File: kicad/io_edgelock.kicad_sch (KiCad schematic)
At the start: 35 parts, among them J1 EdgeLock J1, J2 EdgeLock J2, J3 EdgeLock J3, J4 EdgeLock J4, J5 EdgeLock J5, J6 EdgeLock J6, J9 EdgeLock J9

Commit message: Pick JLCPCB parts for the whole BOM and add BOM/CPL generation
Adds bom/parts.csv (LCSC numbers and MPNs), scripts to apply it to the schematic and
board and to generate the JLCPCB BOM, CPL and a live stock report. Swaps the
BOOTSEL/RESET switch to a basic 5.1 mm part with a matching footprint, and replaces
out-of-stock parts (SS54, WS2812B, 10u caps, SWD header).

Co-Authored-By: Claude Sonnet 5.5 <noreply@anthropic.com>
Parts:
- R44, R45, R46, R47, R48, R49, R50, R51, R52, R53, R54, R55, R56, R57, R58, R59, R60, R61, R62, R63, R64, R65, R66, R67, R68, R69, R70, R71: LCSC (none) -> C25076; MPN (none) -> 0402WGF1000TCE

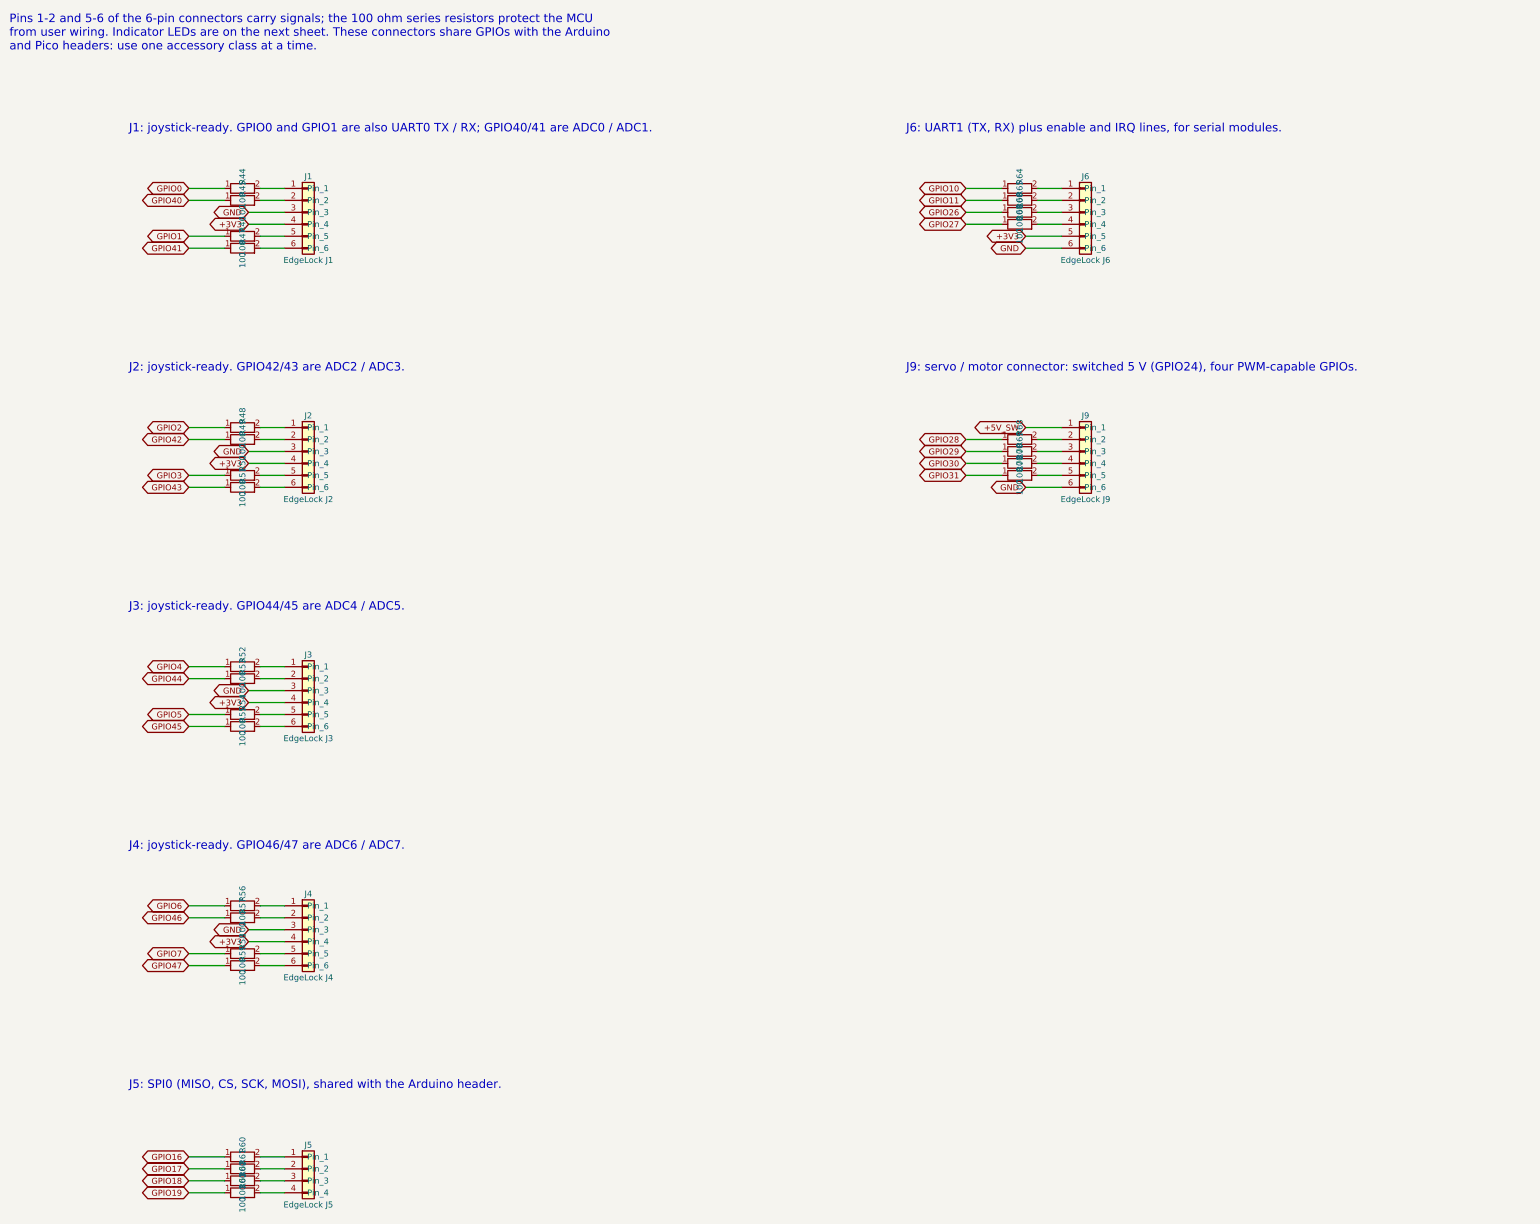
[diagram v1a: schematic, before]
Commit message: Rework board layout, swap SWD header to through-hole, add Qwiic port
- SWD (J10) is now a 1x3 2.54 mm through-hole pin header footprint
  (SWCLK, GND, SWDIO) instead of the JST SH connector; removed from the
  JLCPCB BOM.
- Add J20 Qwiic connector (XY-SM04B-SRSS-TB) on the I2C bus: GND, +3V3,
  GPIO20 (SDA), GPIO21 (SCL), mounting tabs to GND.
- Placement/routing progress and the helper scripts used for it.

DRC still reports open items (unrouted RUN/GPIO24/GPIO29/QSPI_SD0 nets,
R108/GPIO23 and NT1/GPIO20 shorts, J12 edge clearance, silkscreen
overlaps); to be fixed in follow-up commits.

Co-Authored-By: Claude Sonnet 5.5 <noreply@anthropic.com>
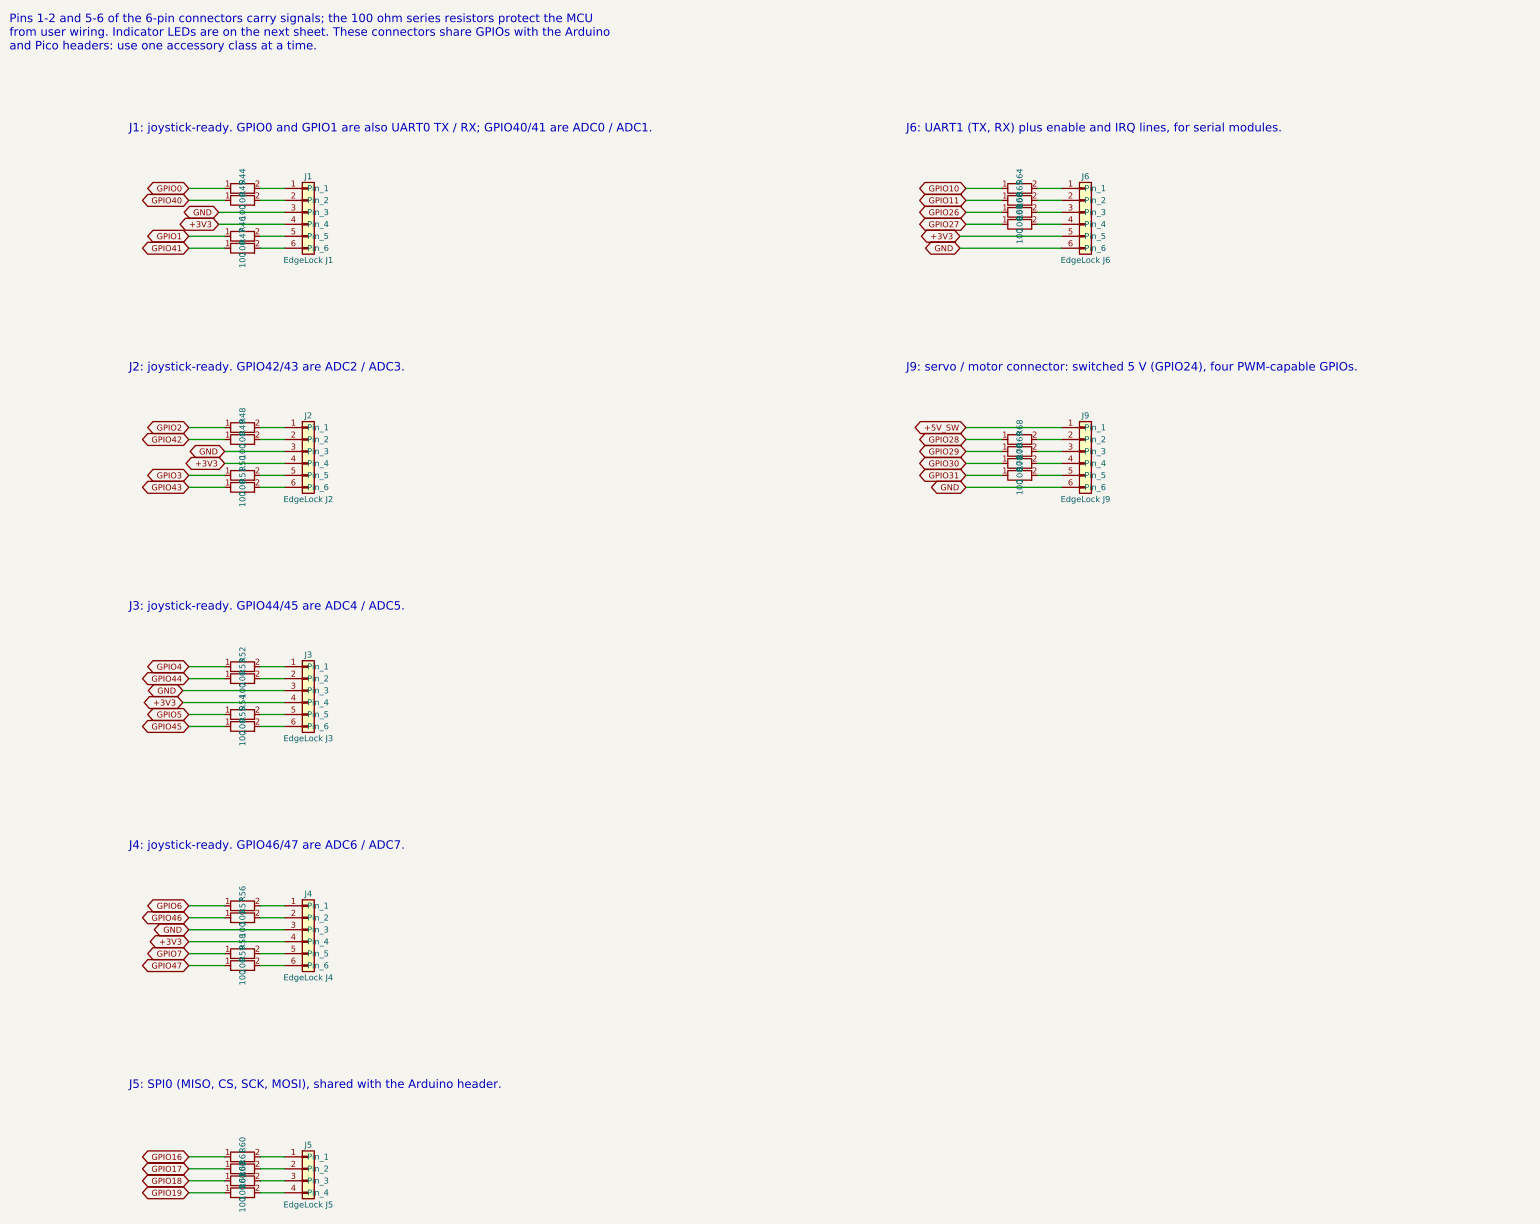
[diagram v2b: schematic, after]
